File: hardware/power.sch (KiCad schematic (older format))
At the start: 0 parts

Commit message: the inputs and power are don for shematic.
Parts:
- added U?: RS-150-48, symbol RS-150-48
- added U?: ZUS104805-A, symbol ZUS104805-A
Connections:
- new net +48V: U?.1 (V+), U?.1 (V+in)
- new net +5V: U?.3 (V+out)
- new net GND: U?.2 (V-), U?.2 (V-in), U?.4 (V-out)
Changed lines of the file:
@@
 LIBS:valves
 LIBS:LDD1500H
+LIBS:power-cache
 EELAYER 25 0
 EELAYER END
@@
 Comment4 ""
 $EndDescr
+$Comp
+L RS-150-48 U?
+U 1 1 5AC2B72E
+P 1250 1400
+F 0 "U?" H 1250 1800 60  0000 C CNN
+F 1 "RS-150-48" H 1250 1800 60  0000 C CNN
+F 2 "" H 1250 1800 60  0000 C CNN
+F 3 "" H 1250 1800 60  0000 C CNN
+	1    1250 1400
+	1    0    0    -1
+$EndComp
+$Comp
+L GND #PWR?
+U 1 1 5AC2B783
+P 1600 1300
+F 0 "#PWR?" H 1600 1050 50  0001 C CNN
+F 1 "GND" H 1600 1150 50  0000 C CNN
+F 2 "" H 1600 1300 50  0000 C CNN
+F 3 "" H 1600 1300 50  0000 C CNN
+	1    1600 1300
+	1    0    0    -1
+$EndComp
+$Comp
+L +48V #PWR?
+U 1 1 5AC2B8CB
+P 1600 1050
+F 0 "#PWR?" H 1600 900 50  0001 C CNN
+F 1 "+48V" H 1600 1190 50  0000 C CNN
+F 2 "" H 1600 1050 50  0000 C CNN
+F 3 "" H 1600 1050 50  0000 C CNN
+	1    1600 1050
+	1    0    0    -1
+$EndComp
+$Comp
+L ZUS104805-A U?
+U 1 1 5AC2D62B
+P 2300 1750
+F 0 "U?" H 2350 2500 60  0000 C CNN
+F 1 "ZUS104805-A" H 2350 2500 60  0000 C CNN
+F 2 "" H 2350 2500 60  0000 C CNN
+F 3 "" H 2350 2500 60  0000 C CNN
+	1    2300 1750
+	1    0    0    -1
+$EndComp
+Wire Wire Line
+	1500 1150 1900 1150
+Wire Wire Line
+	1600 1150 1600 1050
+Connection ~ 1600 1150
+Wire Wire Line
+	1500 1250 1900 1250
+Wire Wire Line
+	1600 1300 1600 1250
+Connection ~ 1600 1250
+$Comp
+L GND #PWR?
+U 1 1 5AC2D6FC
+P 2350 1750
+F 0 "#PWR?" H 2350 1500 50  0001 C CNN
+F 1 "GND" H 2350 1600 50  0000 C CNN
+F 2 "" H 2350 1750 50  0000 C CNN
+F 3 "" H 2350 1750 50  0000 C CNN
+	1    2350 1750
+	1    0    0    -1
+$EndComp
+$Comp
+L GND #PWR?
+U 1 1 5AC2D714
+P 2850 1300
+F 0 "#PWR?" H 2850 1050 50  0001 C CNN
+F 1 "GND" H 2850 1150 50  0000 C CNN
+F 2 "" H 2850 1300 50  0000 C CNN
+F 3 "" H 2850 1300 50  0000 C CNN
+	1    2850 1300
+	1    0    0    -1
+$EndComp
+Wire Wire Line
+	2850 1300 2850 1250
+Wire Wire Line
+	2850 1250 2800 1250
+Wire Wire Line
+	2350 1750 2350 1700
+$Comp
+L +5V #PWR?
+U 1 1 5AC2D745
+P 2850 1100
+F 0 "#PWR?" H 2850 950 50  0001 C CNN
+F 1 "+5V" H 2850 1240 50  0000 C CNN
+F 2 "" H 2850 1100 50  0000 C CNN
+F 3 "" H 2850 1100 50  0000 C CNN
+	1    2850 1100
+	1    0    0    -1
+$EndComp
+Wire Wire Line
+	2800 1150 2850 1150
+Wire Wire Line
+	2850 1150 2850 1100
 $EndSCHEMATC

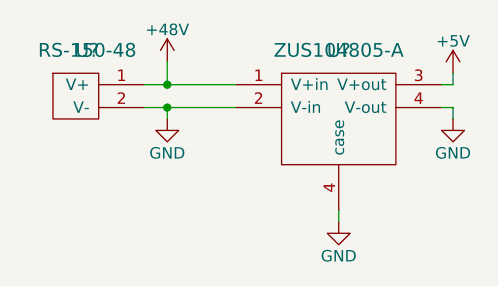
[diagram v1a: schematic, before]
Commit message: sheets are named, global circuit is done.
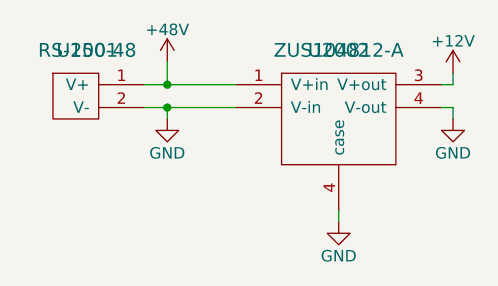
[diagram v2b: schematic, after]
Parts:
- U2002: renamed from U?; value ZUS104805-A -> ZUS104812-A
- gave numbers to parts that had none: 1
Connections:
- net +5V renamed +12V
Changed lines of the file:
@@
 LIBS:contrib
 LIBS:valves
+LIBS:arduino
+LIBS:ESP8266
 LIBS:LDD1500H
-LIBS:power-cache
+LIBS:jardinio-cache
 EELAYER 25 0
 EELAYER END
 $Descr A4 11693 8268
 encoding utf-8
-Sheet 1 1
-Title ""
-Date ""
-Rev ""
-Comp ""
+Sheet 1 5
+Title "jardinIO circuit"
+Date "2018-04-18"
+Rev "0"
+Comp "Cedille"
 Comment1 ""
 Comment2 ""
@@
 $EndDescr
 $Comp
-L RS-150-48 U?
+L RS-150-48 U2001
 U 1 1 5AC2B72E
 P 1250 1400
-F 0 "U?" H 1250 1800 60  0000 C CNN
+F 0 "U2001" H 1250 1800 60  0000 C CNN
 F 1 "RS-150-48" H 1250 1800 60  0000 C CNN
 F 2 "" H 1250 1800 60  0000 C CNN
@@
 $EndComp
 $Comp
-L GND #PWR?
+L GND #PWR01
 U 1 1 5AC2B783
 P 1600 1300
-F 0 "#PWR?" H 1600 1050 50  0001 C CNN
+F 0 "#PWR01" H 1600 1050 50  0001 C CNN
 F 1 "GND" H 1600 1150 50  0000 C CNN
 F 2 "" H 1600 1300 50  0000 C CNN
@@
 $EndComp
 $Comp
-L +48V #PWR?
+L +48V #PWR02
 U 1 1 5AC2B8CB
 P 1600 1050
-F 0 "#PWR?" H 1600 900 50  0001 C CNN
+F 0 "#PWR02" H 1600 900 50  0001 C CNN
 F 1 "+48V" H 1600 1190 50  0000 C CNN
 F 2 "" H 1600 1050 50  0000 C CNN
@@
 $EndComp
 $Comp
-L ZUS104805-A U?
+L ZUS104805-A U2002
 U 1 1 5AC2D62B
 P 2300 1750
-F 0 "U?" H 2350 2500 60  0000 C CNN
-F 1 "ZUS104805-A" H 2350 2500 60  0000 C CNN
+F 0 "U2002" H 2350 2500 60  0000 C CNN
+F 1 "ZUS104812-A" H 2350 2500 60  0000 C CNN
 F 2 "" H 2350 2500 60  0000 C CNN
 F 3 "" H 2350 2500 60  0000 C CNN
@@
 Connection ~ 1600 1250
 $Comp
-L GND #PWR?
+L GND #PWR03
 U 1 1 5AC2D6FC
 P 2350 1750
-F 0 "#PWR?" H 2350 1500 50  0001 C CNN
+F 0 "#PWR03" H 2350 1500 50  0001 C CNN
 F 1 "GND" H 2350 1600 50  0000 C CNN
 F 2 "" H 2350 1750 50  0000 C CNN
@@
 $EndComp
 $Comp
-L GND #PWR?
+L GND #PWR04
 U 1 1 5AC2D714
 P 2850 1300
-F 0 "#PWR?" H 2850 1050 50  0001 C CNN
+F 0 "#PWR04" H 2850 1050 50  0001 C CNN
 F 1 "GND" H 2850 1150 50  0000 C CNN
 F 2 "" H 2850 1300 50  0000 C CNN
@@
 Wire Wire Line
 	2350 1750 2350 1700
+Wire Wire Line
+	2800 1150 2850 1150
+Wire Wire Line
+	2850 1150 2850 1100
 $Comp
-L +5V #PWR?
-U 1 1 5AC2D745
+L +12V #PWR05
+U 1 1 5AD6AF35
 P 2850 1100
-F 0 "#PWR?" H 2850 950 50  0001 C CNN
-F 1 "+5V" H 2850 1240 50  0000 C CNN
+F 0 "#PWR05" H 2850 950 50  0001 C CNN
+F 1 "+12V" H 2850 1240 50  0000 C CNN
 F 2 "" H 2850 1100 50  0000 C CNN
 F 3 "" H 2850 1100 50  0000 C CNN
@@
 	1    0    0    -1
 $EndComp
-Wire Wire Line
-	2800 1150 2850 1150
-Wire Wire Line
-	2850 1150 2850 1100
 $EndSCHEMATC
